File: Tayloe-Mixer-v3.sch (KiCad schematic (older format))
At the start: 60 parts, among them J1 BNC, J101 Audio_Jack, J3 Jack-DC, J4 Conn_01x07_Female, Q1 2N3904-SMD, Q2 2N3904-SMD, SW1 SW_DIP_x01, SW2 Rotary_Encoder_Switch, T1 6:31, T2 31:6, T3 T50_SPLITTER, U1 ESP32-A1S, U2 FST3253, U201 MAR6, U3 LM4562, U4 si5351, U5 L7805, U7 AMS1117CD-3.3

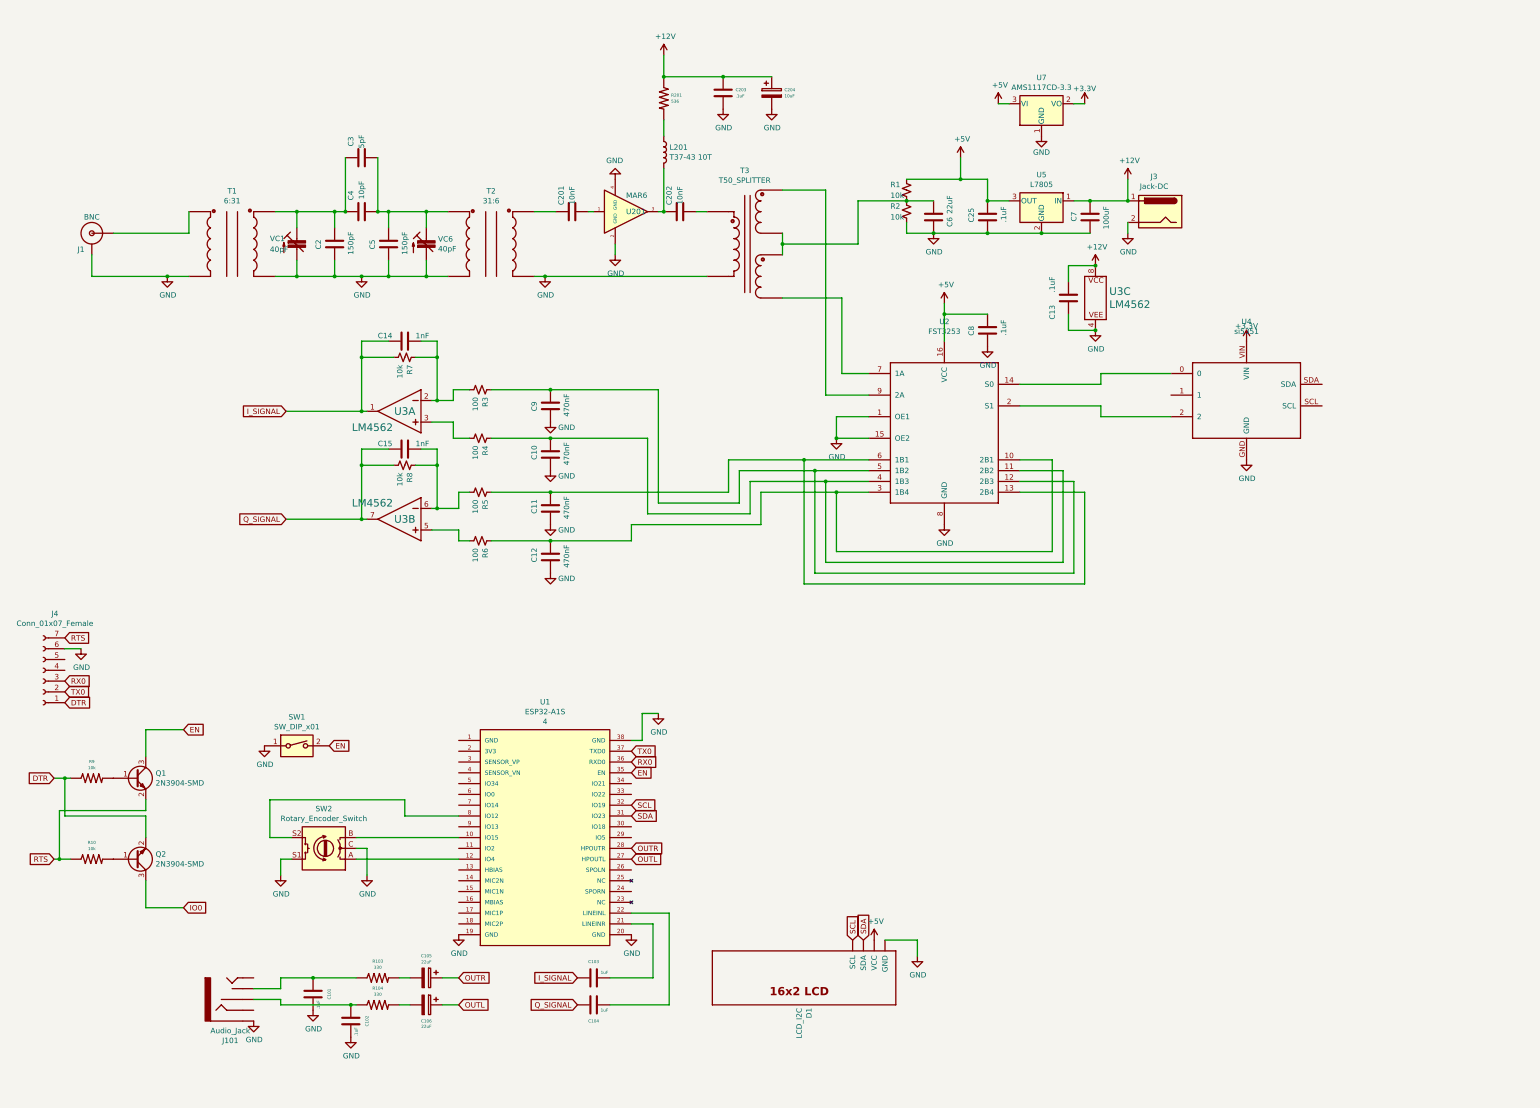
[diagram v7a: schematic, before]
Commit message: updating pcb
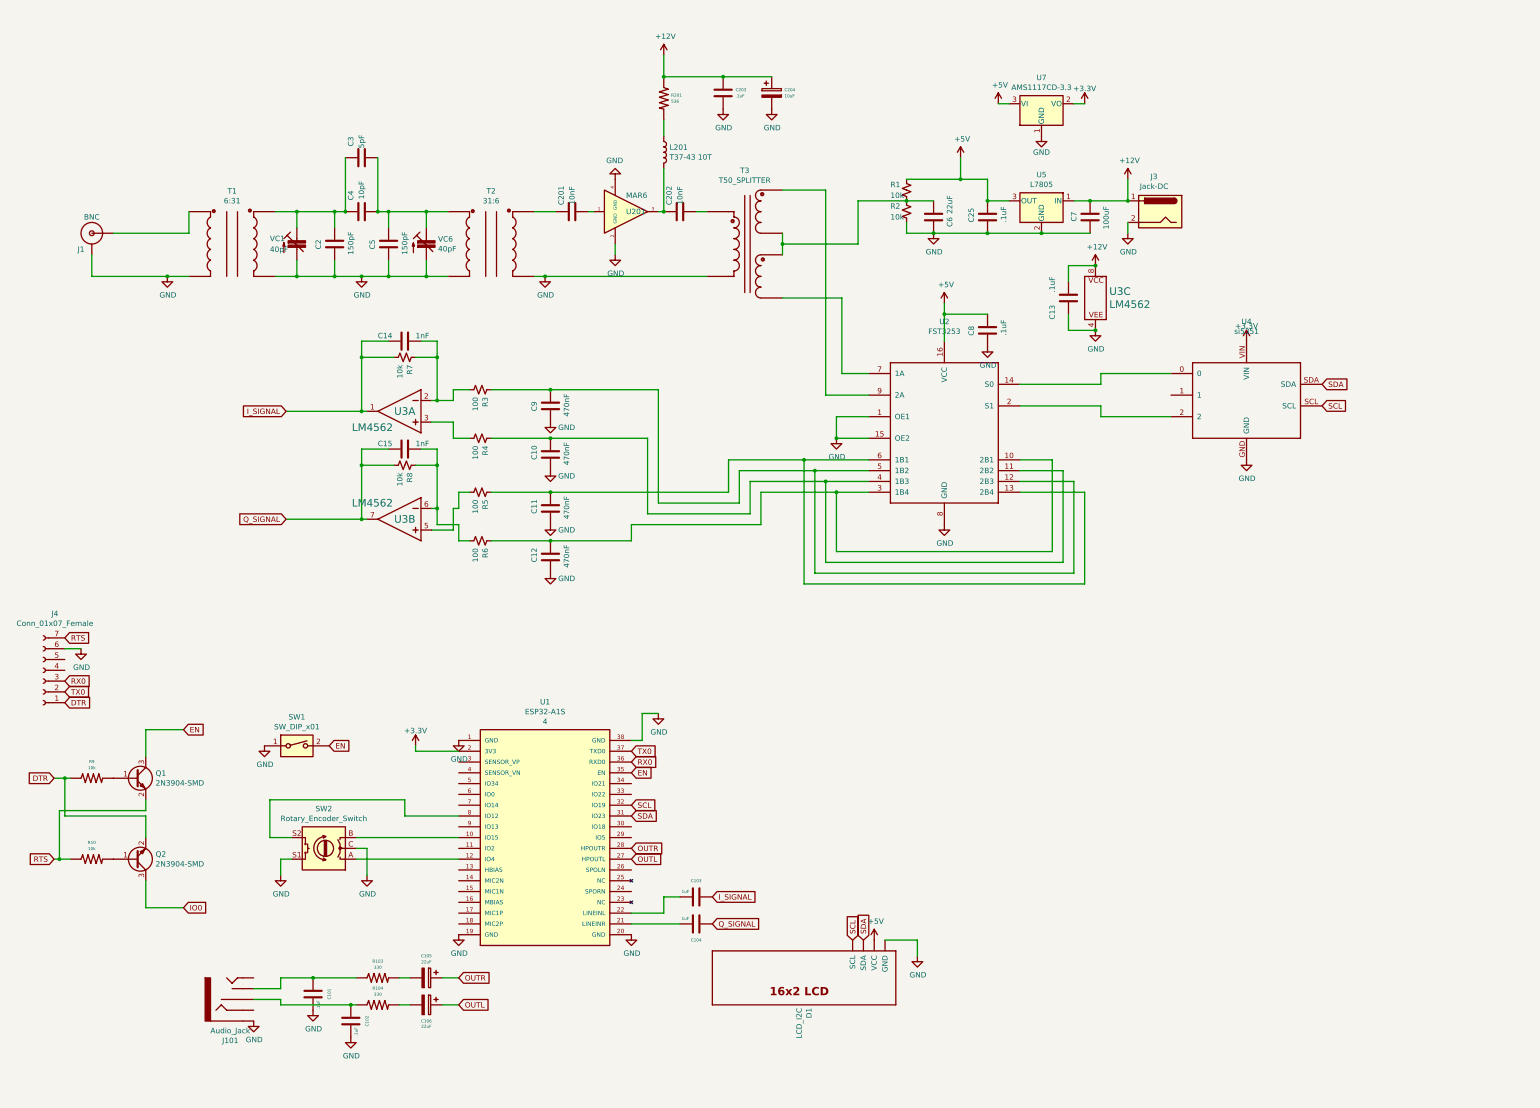
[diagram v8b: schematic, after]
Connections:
- net +3V3: now also U1.2 (3V3)
- net GND: now also U1.1 (GND)
- net SCL: now also U4.SCL
- net SDA: now also U4.SDA
- net at C15.2, R8.1, U3.6 (-IN): now also R6.2; no longer R5.2
- net at U3.5 (+IN): now also R5.2; no longer R6.2
- net at U1.21 (LINEINR): now also C104.2; no longer C103.2
- net at U1.22 (LINEINL): now also C103.2; no longer C104.2
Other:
- moved on the sheet: C103, C104
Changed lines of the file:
@@
 	5150 5250 5150 5400
 Wire Wire Line
-	5150 5400 4950 5400
-Wire Wire Line
 	5250 5700 5150 5700
-Wire Wire Line
-	5150 5700 5150 5600
-Wire Wire Line
-	4900 5600 5150 5600
 $Comp
 L power:GND #PWR010
@@
 Wire Wire Line
 	4950 4850 4950 5000
-Connection ~ 4950 5400
 Wire Wire Line
 	4950 5400 4900 5400
@@
 Wire Wire Line
 	4650 8250 5150 8250
-Text GLabel 6250 10000 0    50   Input ~ 0
+Text GLabel 7500 9250 2    50   Input ~ 0
 Q_SIGNAL
-Text GLabel 6250 9750 0    50   Input ~ 0
+Text GLabel 7500 9000 2    50   Input ~ 0
 I_SIGNAL
 $Comp
 L xenir:Capacitor C103
 U 1 1 62B36FA7
-P 6400 9750
-F 0 "C103" H 6400 9900 28  0000 C CNN
-F 1 "1uF" H 6500 9800 28  0000 C CNN
-F 2 "xenir:Capacitor 1206" H 6400 9600 50  0001 C CNN
-F 3 "" H 6400 9600 50  0001 C CNN
-	1    6400 9750
-	1    0    0    -1
+P 7350 9000
+F 0 "C103" H 7350 8850 28  0000 C CNN
+F 1 "1uF" H 7450 8950 28  0000 C CNN
+F 2 "xenir:Capacitor 1206" H 7350 8850 50  0001 C CNN
+F 3 "" H 7350 8850 50  0001 C CNN
+	1    7350 9000
+	-1   0    0    1
 $EndComp
 $Comp
 L xenir:Capacitor C104
 U 1 1 62B37510
-P 6400 10000
-F 0 "C104" H 6400 9850 28  0000 C CNN
-F 1 "1uF" H 6500 9950 28  0000 C CNN
-F 2 "xenir:Capacitor 1206" H 6400 9850 50  0001 C CNN
-F 3 "" H 6400 9850 50  0001 C CNN
-	1    6400 10000
-	1    0    0    -1
+P 7350 9250
+F 0 "C104" H 7350 9400 28  0000 C CNN
+F 1 "1uF" H 7450 9200 28  0000 C CNN
+F 2 "xenir:Capacitor 1206" H 7350 9100 50  0001 C CNN
+F 3 "" H 7350 9100 50  0001 C CNN
+	1    7350 9250
+	-1   0    0    1
 $EndComp
 Text GLabel 6750 8650 2    50   Input ~ 0
@@
 	1    0    0    -1
 $EndComp
-Wire Wire Line
-	6750 9250 6950 9250
-Wire Wire Line
-	6950 9250 6950 9750
-Wire Wire Line
-	6550 9750 6950 9750
-Wire Wire Line
-	6750 9150 7100 9150
-Wire Wire Line
-	7100 9150 7100 10000
-Wire Wire Line
-	6550 10000 7100 10000
 $Comp
 L xenir:Cap_Polarized C105
@@
 Text GLabel 1500 6600 2    50   Input ~ 0
 RTS
+Wire Wire Line
+	5150 5400 5100 5400
+Wire Wire Line
+	5100 5400 5100 5600
+Wire Wire Line
+	5100 5600 4900 5600
+Wire Wire Line
+	5150 5550 4950 5550
+Wire Wire Line
+	4950 5550 4950 5400
+Wire Wire Line
+	5150 5550 5150 5700
+Connection ~ 4950 5400
+Text GLabel 13150 4450 2    50   Input ~ 0
+SCL
+Text GLabel 13150 4250 2    50   Input ~ 0
+SDA
+Wire Wire Line
+	6750 9150 7050 9150
+Wire Wire Line
+	7050 9150 7050 9000
+Wire Wire Line
+	7050 9000 7200 9000
+Wire Wire Line
+	7200 9250 6750 9250
+$Comp
+L power:+3.3V #PWR0128
+U 1 1 637CA97D
+P 4750 7600
+F 0 "#PWR0128" H 4750 7450 50  0001 C CNN
+F 1 "+3.3V" H 4750 7740 50  0000 C CNN
+F 2 "" H 4750 7600 50  0001 C CNN
+F 3 "" H 4750 7600 50  0001 C CNN
+	1    4750 7600
+	1    0    0    -1
+$EndComp
+Wire Wire Line
+	4750 7600 4750 7650
+Wire Wire Line
+	4750 7650 5150 7650
+$Comp
+L power:GND #PWR0129
+U 1 1 637DEFCC
+P 5150 7550
+F 0 "#PWR0129" H 5150 7300 50  0001 C CNN
+F 1 "GND" H 5155 7377 50  0000 C CNN
+F 2 "" H 5150 7550 50  0001 C CNN
+F 3 "" H 5150 7550 50  0001 C CNN
+	1    5150 7550
+	1    0    0    -1
+$EndComp
 $EndSCHEMATC
